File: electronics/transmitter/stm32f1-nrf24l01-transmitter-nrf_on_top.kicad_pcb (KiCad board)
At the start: 2 copper layers, 86.4 x 38.1 mm, 23 parts, among them K1 CONN_3, K10 CONN_3, K11 CONN_3, K2 CONN_3, K3 CONN_3, K4 CONN_3, K5 CONN_3, K6 CONN_3, K7 CONN_3, K8 CONN_3, K9 CONN_3, P2 LED, P5 CONN_4, Q1 BC548, U1 LIPO_CHARGER_+_PROTECTION, U2 STM32F103C8T6_DEV_BOARD, U3 NRF24L01P

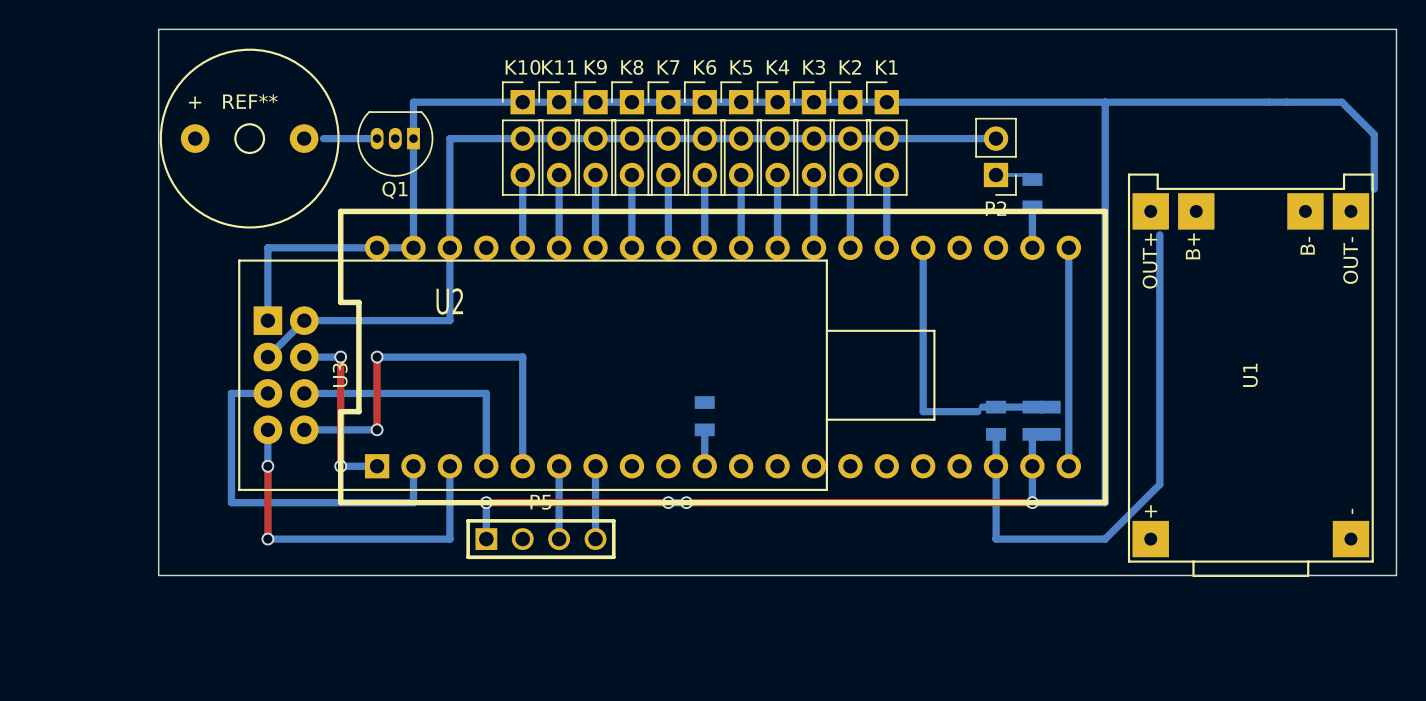
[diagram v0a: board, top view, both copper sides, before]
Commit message: Tweak design to reduce space and wire links
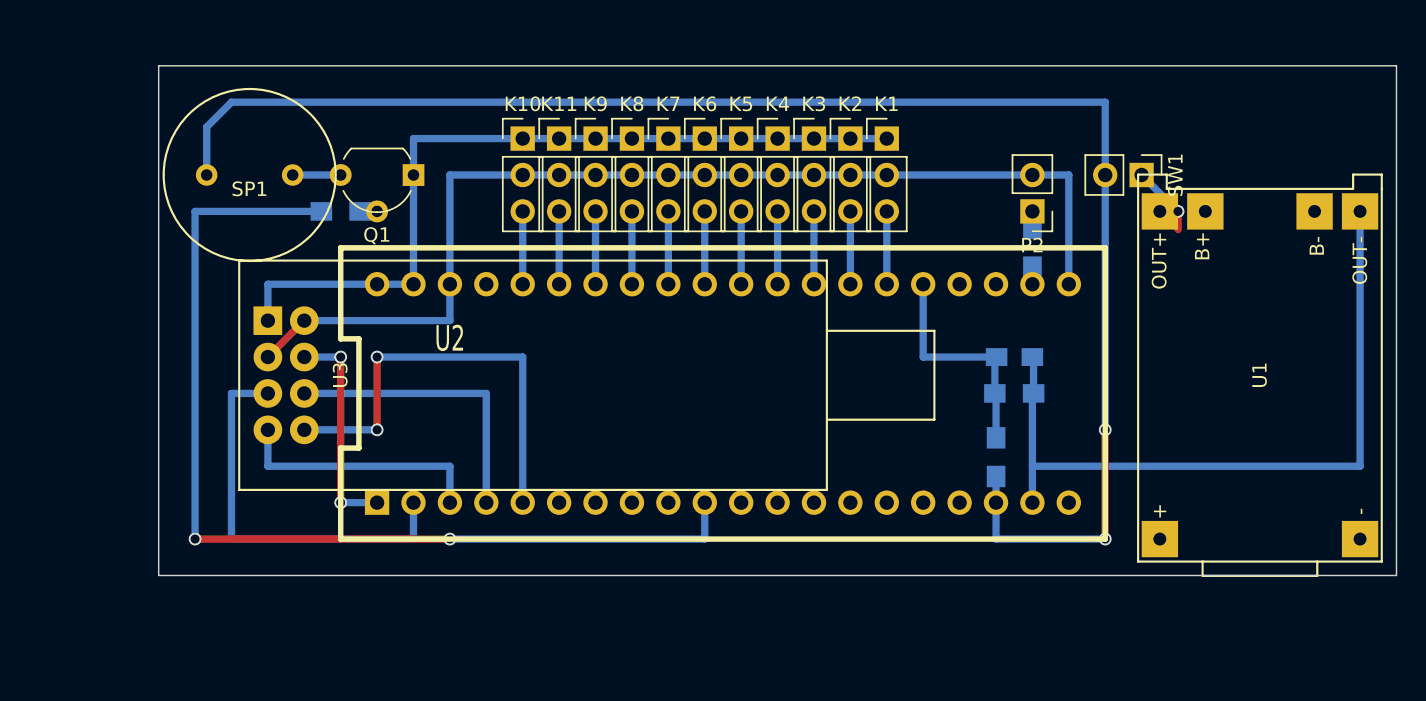
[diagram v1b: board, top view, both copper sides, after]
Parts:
- removed P5: CONN_4, PIN_ARRAY_4x1
- removed REF**: Buzzer_12x9.5RM7.6, Buzzers_Beepers:Buzzer_12x9.5RM7.6
- added SP1: SPEAKER, WLA:Buzzer_passive, F.Cu at (217.2, 111.8)
- added SW1: ON/OFF, Pin_Headers:Pin_Header_Straight_1x02_Pitch2.54mm, F.Cu at (279.4, 111.8)
- C2: footprint SM0805 -> Capacitors_SMD:C_0805_HandSoldering
- Q1: footprint TO_SOT_Packages_THT:TO-92_Inline_Narrow_Oval -> TO_SOT_Packages_THT:TO-92_Molded_Wide
- R1, R4: footprint SM0805 -> Resistors_SMD:R_0805_HandSoldering
- R2: value R -> 22k; footprint SM0805 -> Resistors_SMD:R_0805_HandSoldering
- R3: value R -> 33k; footprint SM0805 -> Resistors_SMD:R_0805_HandSoldering
- moved R4 29.1 mm to (223.5, 114.3), turned to 0 degrees
- moved C2 5.11 mm to (270.5, 124.5), turned to 0 degrees
- moved R1 3.81 mm to (271.8, 116.8)
- moved P2 3.59 mm to (271.8, 114.3)
- moved Q1 2.54 mm to (228.6, 111.8)
- moved U2 2.54 mm to (250.2, 127.0)
- moved K1 2.54 mm to (261.6, 109.2)
- moved K10 2.54 mm to (236.2, 109.2)
- moved K11 2.54 mm to (238.8, 109.2)
- moved K2 2.54 mm to (259.1, 109.2)
- moved K3 2.54 mm to (256.5, 109.2)
- moved K4 2.54 mm to (254.0, 109.2)
- moved K5 2.54 mm to (251.5, 109.2)
- moved K6 2.54 mm to (248.9, 109.2)
- moved K7 2.54 mm to (246.4, 109.2)
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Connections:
- net /ADC1 renamed /PA1/ADC1
- net /ADC2 renamed /PA2/ADC2
- net /ADC3 renamed /PA3/ADC3
- net /ADC4 renamed /PA4/ADC4
- net /ADC5 renamed /PA5/ADC5
- net /ADC6 renamed /PA6/ADC6
- net /ADC7 renamed /PA7/ADC7
- net /ADC8 renamed /PB0/ADC8
- net /ADC9 renamed /PB1/ADC9
- net /SW1 renamed /PB11
- net /SW2 renamed /PB10
- U1 pad 4: N-0000029 -> GND
- U2 pad 11: (no net) -> /PB3
- U2 pad 12: (no net) -> /PB4
- U2 pad 13: (no net) -> /PB5
- U2 pad 14: (no net) -> /PB6
- U2 pad 15: (no net) -> /PB7
- U2 pad 16: (no net) -> /PB8
- U2 pad 17: (no net) -> /PB9
- U2 pad 20: N-0000022 -> Net-(U2-Pad20)
- U2 pad 21: N-0000022 -> VCC
- U2 pad 23: (no net) -> Net-(U2-Pad23)
- U2 pad 24: (no net) -> Net-(U2-Pad24)
- U2 pad 37: (no net) -> Net-(U2-Pad37)
- U2 pad 8: (no net) -> Net-(U2-Pad8)
- U2 pad 9: (no net) -> Net-(U2-Pad9)
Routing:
- net VDD: track 37.7 -> 109.6 mm, vias 0 -> 3
- net GND: track 176.9 -> 106.7 mm, vias 4 -> 0
- net /BUZZER: track 2.54 -> 69.8 mm, vias 0 -> 2
- net N-0000022: track 15.2 -> 0.00 mm
- net VCC: track 65.0 -> 74.7 mm
- net /MISO: track 25.8 -> 17.8 mm, vias 2 -> 0
- net /TX: track 5.08 -> 0.00 mm
- net /RX: track 5.08 -> 0.00 mm
- net Net-(SW1-Pad1): track 0.00 -> 4.86 mm, vias 0 -> 1
- net /ADC0: track 20.5 -> 15.9 mm
- net /CSN: track 12.7 -> 15.6 mm
- net /LED: track 2.86 -> 0.00 mm
- net /SCK: track 25.4 -> 27.9 mm
- net /MOSI: track 17.8 -> 20.3 mm
- net /IRQ: track 27.9 -> 30.5 mm
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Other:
- board size 86.4 x 38.1 mm -> 86.4 x 35.6 mm
- board text added: "1"
- board text added: "10"
- board text added: "13"
- board text added: "15"
- board text added: "20"
- board text added: "25"
- board text added: "30"
- board text added: "33"
- board text added: "5"

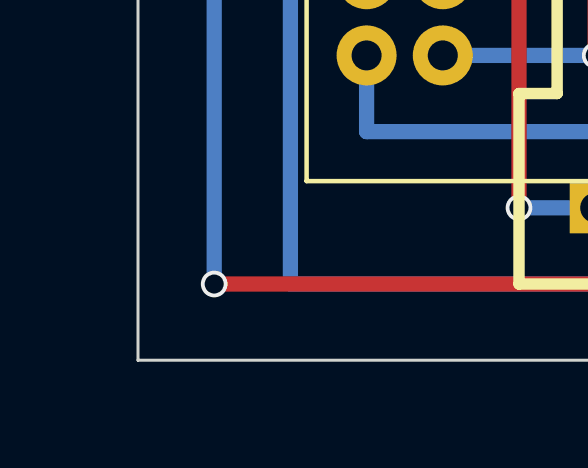
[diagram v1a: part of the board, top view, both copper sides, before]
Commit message: Add mechanical mounting via dummy fiducial
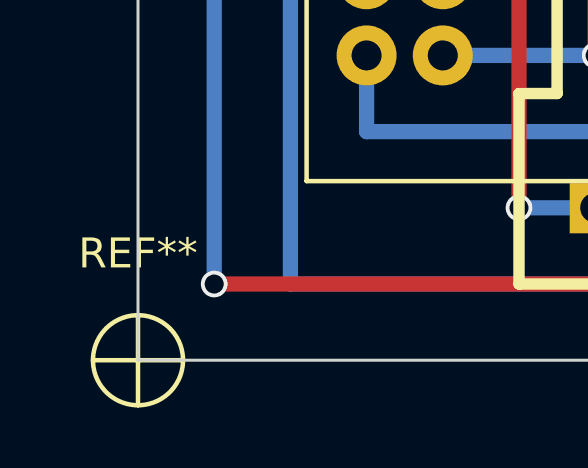
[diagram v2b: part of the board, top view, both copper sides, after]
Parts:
- added REF**: Fiducial_classic_Small_SilkscreenTop_Type1, Fiducials:Fiducial_classic_Small_SilkscreenTop_Type1, F.Cu at (210.8, 139.7)
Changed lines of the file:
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@@
 (kicad_pcb (version 4) (host pcbnew 4.0.5-e0-6337~49~ubuntu16.04.1)
   (general
-    (links 61)
-    (no_connects 5)
-    (area 206.851429 100.4 301.148571 143.59)
+    (links 0)
+    (no_connects 4)
+    (area 124.409295 139.666417 210.869297 175.326419)
     (thickness 1.6)
     (drawings 28)
     (tracks 103)
     (zones 0)
-    (modules 23)
+    (modules 24)
     (nets 46)
   )
@@
   )
   (setup
-    (last_trace_width 0.508)
+    (last_trace_width 0.254)
     (user_trace_width 0.508)
     (trace_clearance 0.1016)
@@
     (pad_to_mask_clearance 0)
     (aux_axis_origin 210.82 139.7)
-    (visible_elements 7FFFFF3F)
+    (visible_elements 7FFFEF3F)
     (pcbplotparams
       (layerselection 0x00030_80000001)
@@
     (add_net VDD)
   )
+  (module Fiducials:Fiducial_classic_Small_SilkscreenTop_Type1 (layer F.Cu)
+    (at 210.82 139.7)
+    (descr "Fiducial, Classical, Small, Copper Top, Typ 1, Passermarke,")
+    (tags "Fiducial, Classical, Small, Copper Top, Typ 1, Passermarke,")
+    (fp_text reference REF** (at 0 -3.556) (layer F.SilkS)
+      (effects (font (size 1 1) (thickness 0.15)))
+    )
+    (fp_text value Fiducial_classic_Small_SilkscreenTop_Type1 (at 0.34036 3.4798) (layer F.Fab)
+      (effects (font (size 1 1) (thickness 0.15)))
+    )
+    (fp_line (start -1.50114 0) (end 1.50114 0) (layer F.SilkS) (width 0.15))
+    (fp_line (start 0 -1.50114) (end 0 1.50114) (layer F.SilkS) (width 0.15))
+    (fp_circle (center 0 0) (end 1.50114 0) (layer F.SilkS) (width 0.15))
+    (pad ~ smd circle (at 0 0) (size 4.50088 4.50088) (layers F.Mask)
+      (solder_mask_margin 2.99974))
+    (model /home/laneboysrc/projects/3D-printed-parts/headless-tx/mount.x3d
+      (at (xyz 0 0 0))
+      (scale (xyz 1 1 1))
+      (rotate (xyz 0 0 0))
+    )
+  )
   (module WLA:NRF24L01P-PA-LNA (layer F.Cu)
     (at 218.44 125.73 270)
@@
     )
   )
-  (gr_text 15 (at 248.92 101.6) (layer Cmts.User)
-    (effects (font (size 1.5 1.5) (thickness 0.3)))
-  )
-  (gr_text 10 (at 236.22 101.6) (layer Cmts.User)
-    (effects (font (size 1.5 1.5) (thickness 0.3)))
-  )
-  (gr_text 5 (at 223.52 101.6) (layer Cmts.User)
-    (effects (font (size 1.5 1.5) (thickness 0.3)))
-  )
-  (gr_text 1 (at 213.36 101.6) (layer Cmts.User)
-    (effects (font (size 1.5 1.5) (thickness 0.3)))
-  )
-  (gr_text 33 (at 294.64 101.6) (layer Cmts.User)
-    (effects (font (size 1.5 1.5) (thickness 0.3)))
-  )
-  (gr_text 30 (at 287.02 101.6) (layer Cmts.User)
-    (effects (font (size 1.5 1.5) (thickness 0.3)))
-  )
-  (gr_text 25 (at 274.32 101.6) (layer Cmts.User)
-    (effects (font (size 1.5 1.5) (thickness 0.3)))
-  )
-  (gr_text 20 (at 261.62 101.6) (layer Cmts.User)
-    (effects (font (size 1.5 1.5) (thickness 0.3)))
-  )
-  (gr_text 13 (at 299.72 106.68) (layer Cmts.User)
-    (effects (font (size 1.5 1.5) (thickness 0.3)))
-  )
-  (gr_text 10 (at 299.72 114.3) (layer Cmts.User)
-    (effects (font (size 1.5 1.5) (thickness 0.3)))
-  )
-  (gr_text 5 (at 299.72 127) (layer Cmts.User)
-    (effects (font (size 1.5 1.5) (thickness 0.3)))
-  )
-  (gr_text 1 (at 299.72 137.16) (layer Cmts.User)
-    (effects (font (size 1.5 1.5) (thickness 0.3)))
-  )
-  (gr_text 13 (at 208.28 106.68) (layer Cmts.User)
-    (effects (font (size 1.5 1.5) (thickness 0.3)))
-  )
-  (gr_text 10 (at 208.28 114.3) (layer Cmts.User)
-    (effects (font (size 1.5 1.5) (thickness 0.3)))
-  )
-  (gr_text 5 (at 208.28 127) (layer Cmts.User)
-    (effects (font (size 1.5 1.5) (thickness 0.3)))
-  )
-  (gr_text 1 (at 208.28 137.16) (layer Cmts.User)
-    (effects (font (size 1.5 1.5) (thickness 0.3)))
-  )
-  (gr_text 33 (at 294.64 142.24) (layer Cmts.User)
-    (effects (font (size 1.5 1.5) (thickness 0.3)))
-  )
-  (gr_text 30 (at 287.02 142.24) (layer Cmts.User)
-    (effects (font (size 1.5 1.5) (thickness 0.3)))
-  )
-  (gr_text 25 (at 274.32 142.24) (layer Cmts.User)
-    (effects (font (size 1.5 1.5) (thickness 0.3)))
-  )
-  (gr_text 20 (at 261.62 142.24) (layer Cmts.User)
-    (effects (font (size 1.5 1.5) (thickness 0.3)))
-  )
-  (gr_text 15 (at 248.92 142.24) (layer Cmts.User)
-    (effects (font (size 1.5 1.5) (thickness 0.3)))
-  )
-  (gr_text 10 (at 236.22 142.24) (layer Cmts.User)
-    (effects (font (size 1.5 1.5) (thickness 0.3)))
-  )
-  (gr_text 5 (at 223.52 142.24) (layer Cmts.User)
-    (effects (font (size 1.5 1.5) (thickness 0.3)))
-  )
-  (gr_text 1 (at 213.36 142.24) (layer Cmts.User)
-    (effects (font (size 1.5 1.5) (thickness 0.3)))
-  )
+  (gr_text 15 (at 248.92 101.6 -360) (layer Cmts.User)
+    (effects (font (size 1.5 1.5) (thickness 0.3)))
+  )
+  (gr_text 10 (at 236.22 101.6 -360) (layer Cmts.User)
+    (effects (font (size 1.5 1.5) (thickness 0.3)))
+  )
+  (gr_text 5 (at 223.52 101.6 -360) (layer Cmts.User)
+    (effects (font (size 1.5 1.5) (thickness 0.3)))
+  )
+  (gr_text 1 (at 213.36 101.6 -360) (layer Cmts.User)
+    (effects (font (size 1.5 1.5) (thickness 0.3)))
+  )
+  (gr_text 33 (at 294.64 101.6 -360) (layer Cmts.User)
+    (effects (font (size 1.5 1.5) (thickness 0.3)))
+  )
+  (gr_text 30 (at 287.02 101.6 -360) (layer Cmts.User)
+    (effects (font (size 1.5 1.5) (thickness 0.3)))
+  )
+  (gr_text 25 (at 274.32 101.6 -360) (layer Cmts.User)
+    (effects (font (size 1.5 1.5) (thickness 0.3)))
+  )
+  (gr_text 20 (at 261.62 101.6 -360) (layer Cmts.User)
+    (effects (font (size 1.5 1.5) (thickness 0.3)))
+  )
+  (gr_text 13 (at 299.72 106.68 -360) (layer Cmts.User)
+    (effects (font (size 1.5 1.5) (thickness 0.3)))
+  )
+  (gr_text 10 (at 299.72 114.3 -360) (layer Cmts.User)
+    (effects (font (size 1.5 1.5) (thickness 0.3)))
+  )
+  (gr_text 5 (at 299.72 127 -360) (layer Cmts.User)
+    (effects (font (size 1.5 1.5) (thickness 0.3)))
+  )
+  (gr_text 1 (at 299.72 137.16 -360) (layer Cmts.User)
+    (effects (font (size 1.5 1.5) (thickness 0.3)))
+  )
+  (gr_text 13 (at 208.28 106.68 -360) (layer Cmts.User)
+    (effects (font (size 1.5 1.5) (thickness 0.3)))
+  )
+  (gr_text 10 (at 208.28 114.3 -360) (layer Cmts.User)
+    (effects (font (size 1.5 1.5) (thickness 0.3)))
+  )
+  (gr_text 5 (at 208.28 127 -360) (layer Cmts.User)
+    (effects (font (size 1.5 1.5) (thickness 0.3)))
+  )
+  (gr_text 1 (at 208.28 137.16 -360) (layer Cmts.User)
+    (effects (font (size 1.5 1.5) (thickness 0.3)))
+  )
+  (gr_text 33 (at 294.64 142.24 -360) (layer Cmts.User)
+    (effects (font (size 1.5 1.5) (thickness 0.3)))
+  )
+  (gr_text 30 (at 287.02 142.24 -360) (layer Cmts.User)
+    (effects (font (size 1.5 1.5) (thickness 0.3)))
+  )
+  (gr_text 25 (at 274.32 142.24 -360) (layer Cmts.User)
+    (effects (font (size 1.5 1.5) (thickness 0.3)))
+  )
+  (gr_text 20 (at 261.62 142.24 -360) (layer Cmts.User)
+    (effects (font (size 1.5 1.5) (thickness 0.3)))
+  )
+  (gr_text 15 (at 248.92 142.24 -360) (layer Cmts.User)
+    (effects (font (size 1.5 1.5) (thickness 0.3)))
+  )
+  (gr_text 10 (at 236.22 142.24 -360) (layer Cmts.User)
+    (effects (font (size 1.5 1.5) (thickness 0.3)))
+  )
+  (gr_text 5 (at 223.52 142.24 -360) (layer Cmts.User)
+    (effects (font (size 1.5 1.5) (thickness 0.3)))
+  )
+  (gr_text 1 (at 213.36 142.24 -360) (layer Cmts.User)
+    (effects (font (size 1.5 1.5) (thickness 0.3)))
+  )

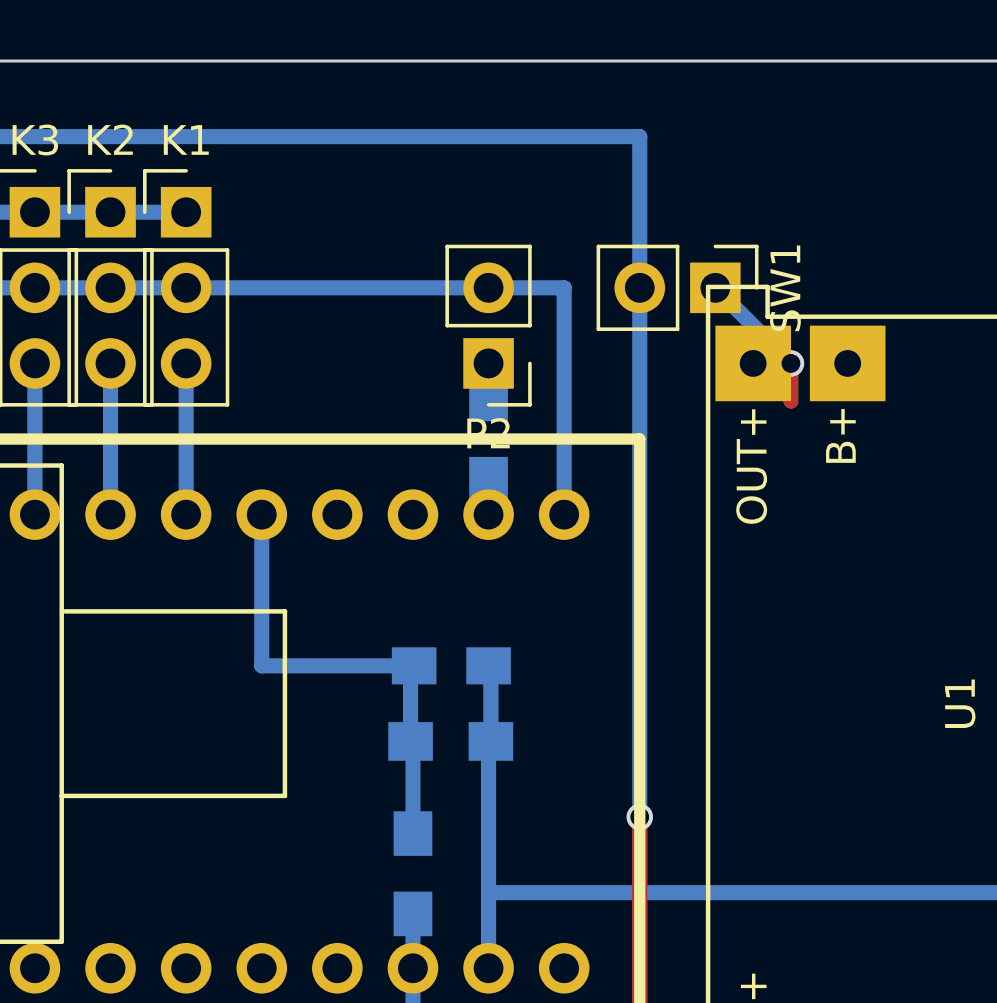
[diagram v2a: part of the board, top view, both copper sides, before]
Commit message: Fix switch connector overlapping with charger
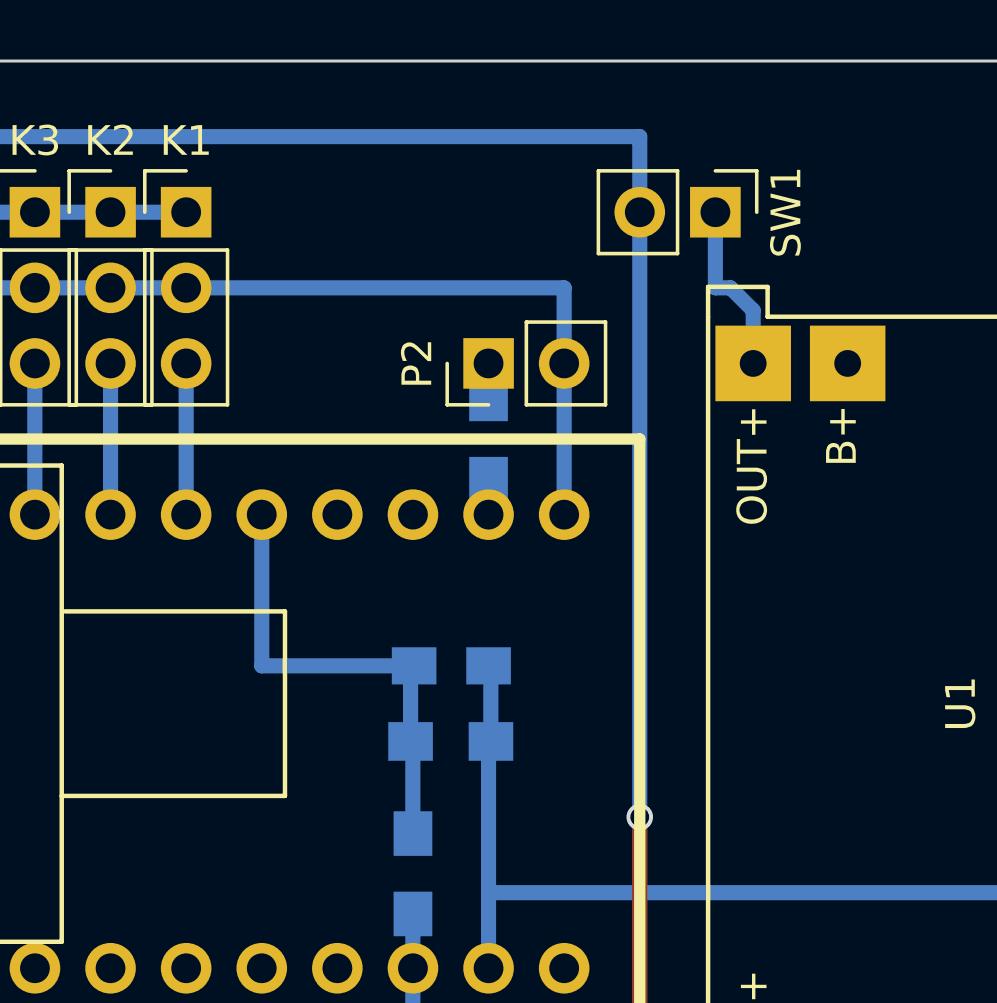
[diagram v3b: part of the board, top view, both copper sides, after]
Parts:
- moved SW1 2.54 mm to (279.4, 109.2)
- turned P2 to 90 degrees
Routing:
- net Net-(SW1-Pad1): track 4.86 -> 5.90 mm, vias 1 -> 0
- net VDD: vias 3 -> 2
